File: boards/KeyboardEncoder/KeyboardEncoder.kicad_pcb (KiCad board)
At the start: 2 copper layers, 150 x 100 mm, 29 parts, among them J1 ISP, J2 Encoder, J3 MIDI Out, J4 SelectRX, J5 MIDI In, J7 BoardCon, J8 PistonEncoder, U1 ATmega48-20P, U2 6N137, U4 L7805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

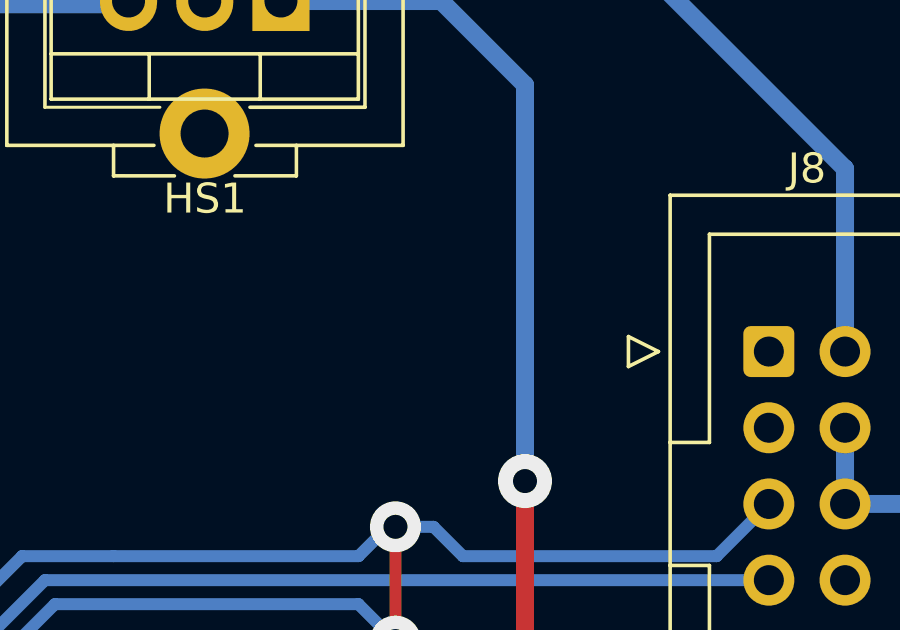
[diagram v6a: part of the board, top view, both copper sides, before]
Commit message: Added bypass caps to power supplies, use cheaper MAX232 IC.
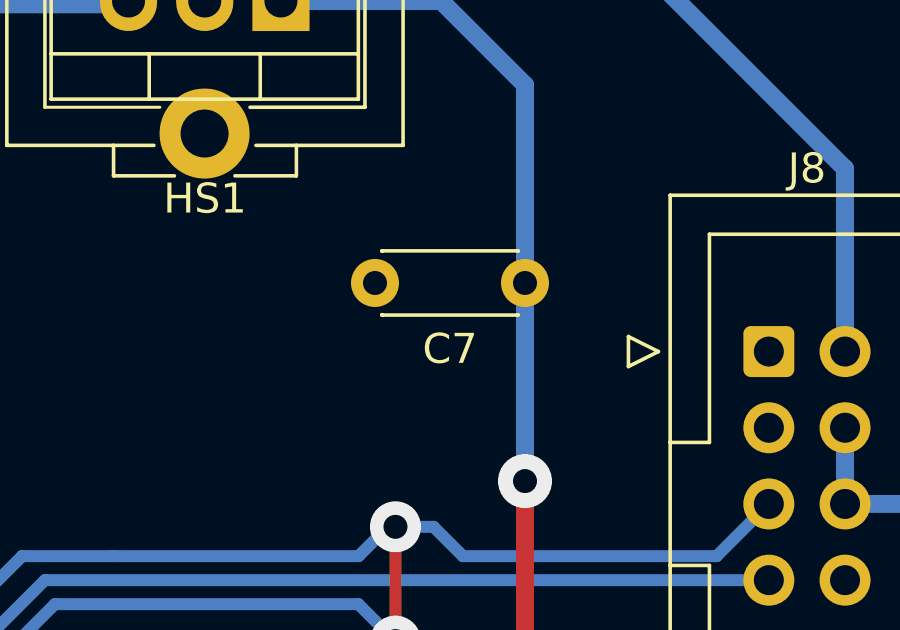
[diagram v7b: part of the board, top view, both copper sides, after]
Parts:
- added C7: 330nF, Capacitor_THT:C_Disc_D4.3mm_W1.9mm_P5.00mm, F.Cu at (201.4, 105.7)
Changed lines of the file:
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@@
+		)
+	)
+	(footprint "Capacitor_THT:C_Disc_D4.3mm_W1.9mm_P5.00mm"
+		(layer "F.Cu")
+		(at 201.422 105.664 180)
+		(descr "C, Disc series, Radial, pin pitch=5.00mm, , diameter*width=4.3*1.9mm^2, Capacitor, http://www.vishay.com/docs/45233/krseries.pdf")
+		(tags "C Disc series Radial pin pitch 5.00mm  diameter 4.3mm width 1.9mm Capacitor")
+		(property "Reference" "C7"
+			(at 2.5 -2.2 180)
+			(layer "F.SilkS")
+			(effects
+				(font
+					(size 1 1)
+					(thickness 0.15)
+				)
+			)
+		)
+		(property "Value" "330nF"
+			(at 2.5 2.2 180)
+			(layer "F.Fab")
+			(effects
+				(font
+					(size 1 1)
+					(thickness 0.15)
+				)
+			)
+		)
+		(property "Footprint" "Capacitor_THT:C_Disc_D4.3mm_W1.9mm_P5.00mm"
+			(at 0 0 180)
+			(unlocked yes)
+			(layer "F.Fab")
+			(hide yes)
+			(effects
+				(font
+					(size 1.27 1.27)
+				)
+			)
+		)
+		(property "Datasheet" ""
+			(at 0 0 180)
+			(unlocked yes)
+			(layer "F.Fab")
+			(hide yes)
+			(effects
+				(font
+					(size 1.27 1.27)
+				)
+			)
+		)
+		(property "Description" "Unpolarized capacitor"
+			(at 0 0 180)
+			(unlocked yes)
+			(layer "F.Fab")
+			(hide yes)
+			(effects
+				(font
+					(size 1.27 1.27)
+				)
+			)
+		)
+		(property ki_fp_filters "C_*")
+		(sheetname "Root")
+		(sheetfile "KeyboardEncoder.kicad_sch")
+		(attr through_hole)
+		(fp_line
+			(start 4.77 1.055)
+			(end 4.77 1.07)
+			(stroke
+				(width 0.12)
+				(type solid)
+			)
+			(layer "F.SilkS")
+		)
+		(fp_line
+			(start 4.77 -1.07)
+			(end 4.77 -1.055)
+			(stroke
+				(width 0.12)
+				(type solid)
+			)
+			(layer "F.SilkS")
+		)
+		(fp_line
+			(start 0.23 1.07)
+			(end 4.77 1.07)
+			(stroke
+				(width 0.12)
+				(type solid)
+			)
+			(layer "F.SilkS")
+		)
+		(fp_line
+			(start 0.23 1.055)
+			(end 0.23 1.07)
+			(stroke
+				(width 0.12)
+				(type solid)
+			)
+			(layer "F.SilkS")
+		)
+		(fp_line
+			(start 0.23 -1.07)
+			(end 4.77 -1.07)
+			(stroke
+				(width 0.12)
+				(type solid)
+			)
+			(layer "F.SilkS")
+		)
+		(fp_line
+			(start 0.23 -1.07)
+			(end 0.23 -1.055)
+			(stroke
+				(width 0.12)
+				(type solid)
+			)
+			(layer "F.SilkS")
+		)
+		(fp_line
+			(start 6.05 1.2)
+			(end 6.05 -1.2)
+			(stroke
+				(width 0.05)
+				(type solid)
+			)
+			(layer "F.CrtYd")
+		)
+		(fp_line
+			(start 6.05 -1.2)
+			(end -1.05 -1.2)
+			(stroke
+				(width 0.05)
+				(type solid)
+			)
+			(layer "F.CrtYd")
+		)
+		(fp_line
+			(start -1.05 1.2)
+			(end 6.05 1.2)
+			(stroke
+				(width 0.05)
+				(type solid)
+			)
+			(layer "F.CrtYd")
+		)
+		(fp_line
+			(start -1.05 -1.2)
+			(end -1.05 1.2)
+			(stroke
+				(width 0.05)
+				(type solid)
+			)
+			(layer "F.CrtYd")
+		)
+		(fp_line
+			(start 4.65 0.95)
+			(end 4.65 -0.95)
+			(stroke
+				(width 0.1)
+				(type solid)
+			)
+			(layer "F.Fab")
+		)
+		(fp_line
+			(start 4.65 -0.95)
+			(end 0.35 -0.95)
+			(stroke
+				(width 0.1)
+				(type solid)
+			)
+			(layer "F.Fab")
+		)
+		(fp_line
+			(start 0.35 0.95)
+			(end 4.65 0.95)
+			(stroke
+				(width 0.1)
+				(type solid)
+			)
+			(layer "F.Fab")
+		)
+		(fp_line
+			(start 0.35 -0.95)
+			(end 0.35 0.95)
+			(stroke
+				(width 0.1)
+				(type solid)
+			)
+			(layer "F.Fab")
+		)
+		(fp_text user "${REFERENCE}"
+			(at 2.5 0 180)
+			(layer "F.Fab")
+			(effects
+				(font
+					(size 0.86 0.86)
+					(thickness 0.129)
+				)
+			)
+		)
+		(pad "1" thru_hole circle
+			(at 0 0 180)
+			(size 1.6 1.6)
+			(drill 0.8)
+			(layers "*.Cu" "*.Mask")
+			(remove_unused_layers no)
+			(net 28 "+12V")
+			(pintype "passive")
+		)
+		(pad "2" thru_hole circle
+			(at 5 0 180)
+			(size 1.6 1.6)
+			(drill 0.8)
+			(layers "*.Cu" "*.Mask")
+			(remove_unused_layers no)
+			(net 2 "GND")
+			(pintype "passive")
+		)
+		(model "${KICAD8_3DMODEL_DIR}/Capacitor_THT.3dshapes/C_Disc_D4.3mm_W1.9mm_P5.00mm.wrl"
+			(offset
+				(xyz 0 0 0)
+			)
+			(scale
+				(xyz 1 1 1)
+			)
+			(rotate
+				(xyz 0 0 0)
+			)
 		)
 	)

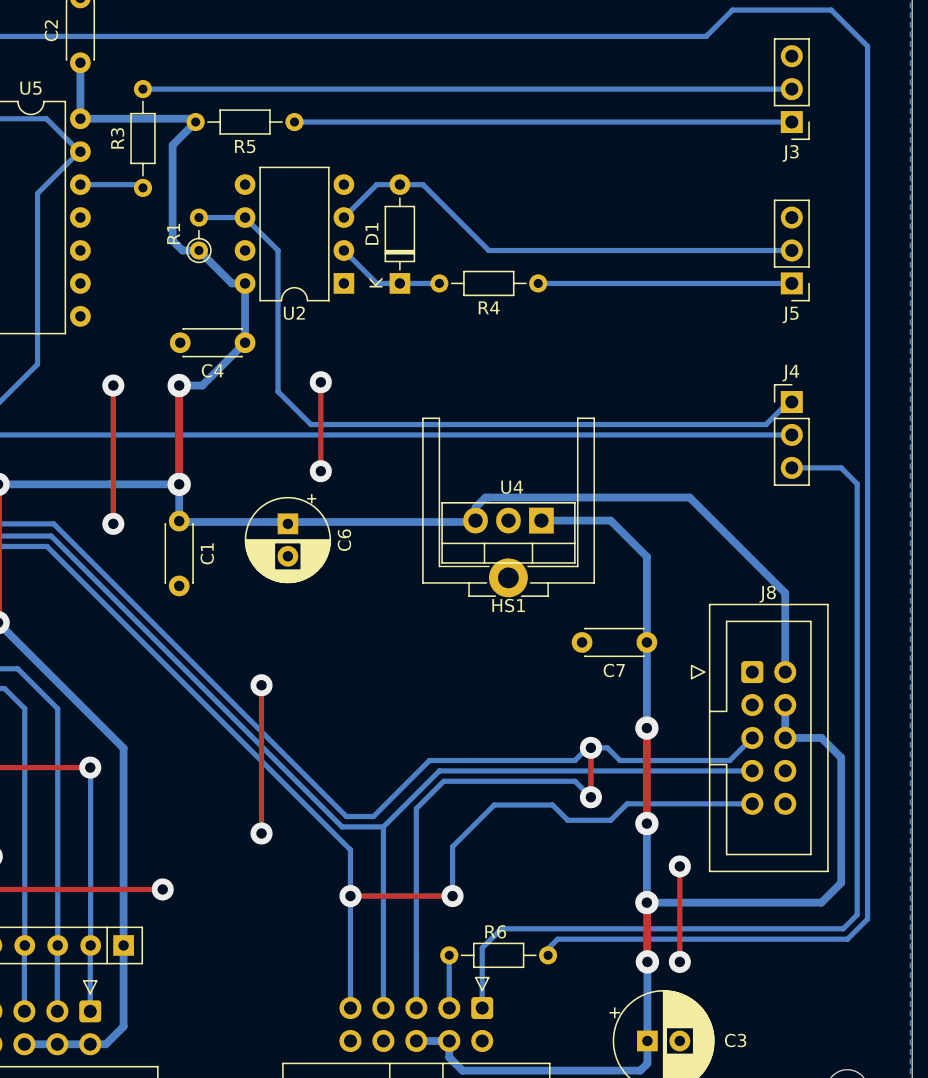
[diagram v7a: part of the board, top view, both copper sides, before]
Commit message: Updated design rules to 0.32mm template and exported Gerber files
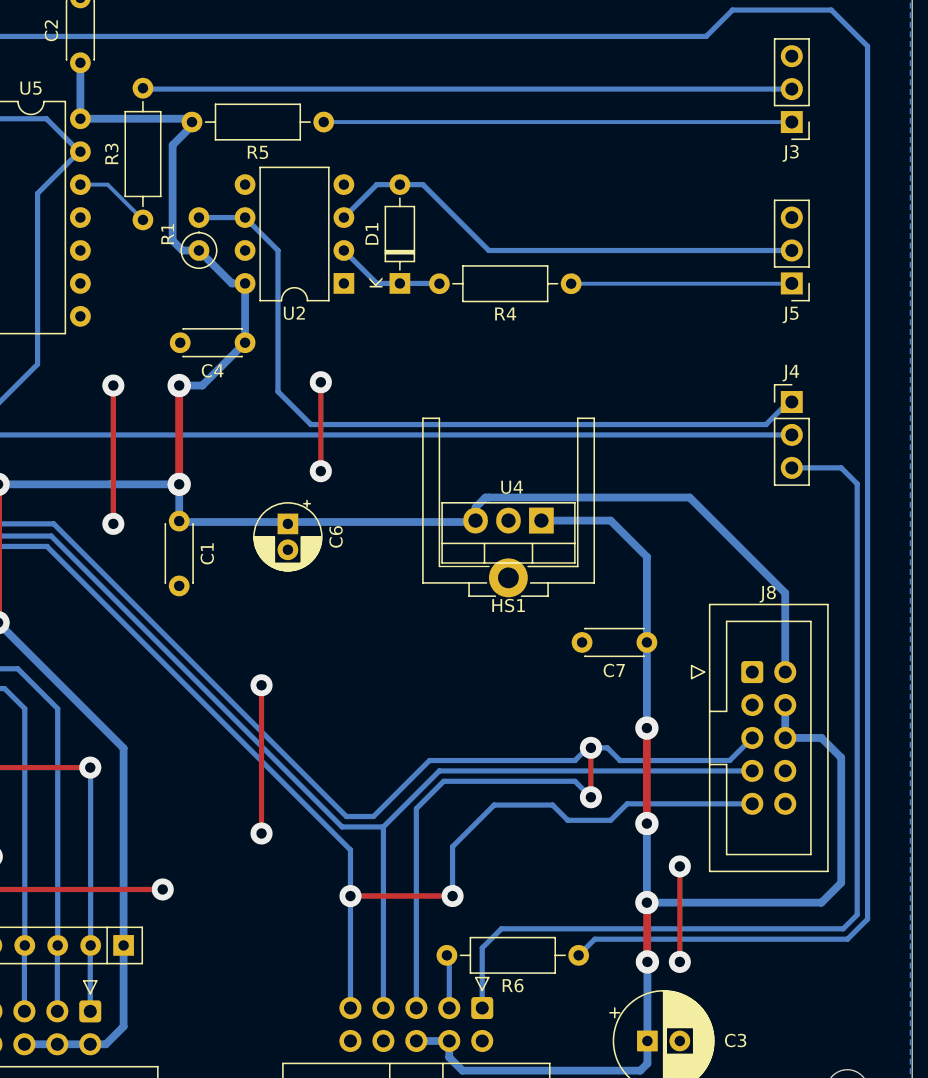
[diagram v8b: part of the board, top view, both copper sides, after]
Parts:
- C6: footprint Capacitor_THT:CP_Radial_D6.3mm_P2.50mm -> Capacitor_THT:CP_Radial_D5.0mm_P2.00mm
- R1: footprint Resistor_THT:R_Axial_DIN0204_L3.6mm_D1.6mm_P2.54mm_Vertical -> Resistor_THT:R_Axial_DIN0207_L6.3mm_D2.5mm_P2.54mm_Vertical
- R3, R4, R5, R6: footprint Resistor_THT:R_Axial_DIN0204_L3.6mm_D1.6mm_P7.62mm_Horizontal -> Resistor_THT:R_Axial_DIN0207_L6.3mm_D2.5mm_P10.16mm_Horizontal
- moved R4 2.54 mm to (195.6, 78.0)
- moved R3 2.47 mm to (162.6, 73.1)
- moved R6 2.36 mm to (196.2, 129.8)
- moved R5 2.26 mm to (176.5, 65.5)
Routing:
- net Net-(R6-Pad1): track 174.5 -> 171.9 mm
- net Net-(J5-Pin_1): track 19.6 -> 17.0 mm
- net Net-(J3-Pin_1): track 38.4 -> 36.1 mm
- net Net-(R3-Pad1): track 5.01 -> 5.95 mm
